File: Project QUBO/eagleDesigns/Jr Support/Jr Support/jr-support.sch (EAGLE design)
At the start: 173 parts, among them U1 PCA9685, U2 BME280

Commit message: 
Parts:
- added LED1, LED2, LED3, LED4, LED5, LED6, LED7: (no value), led:0805_LED
- added R20, R29, R32: 1.5k, resistor:R-US_R0805
- added R30, R31: 270, resistor:R-US_R0805
- added R33: 1.2k, resistor:R-US_R0805
- added R34: 68, resistor:R-US_R0805
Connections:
- new net N$68: LED1.A, R20.1
- new net N$69: LED2.A, R29.1
- new net N$70: LED3.A, R30.1
- new net N$71: LED4.A, R31.1
- new net N$72: LED5.A, R32.1
- new net N$73: LED6.A, R33.1
- new net N$74: LED7.A, R34.1
- net 12V: now also R33.2
- net GND: now also LED1.C, LED2.C, LED3.C, LED4.C, LED5.C, LED6.C, LED7.C
- net RELAY_OUT: now also R20.2
- net V_THRUST: now also R32.2
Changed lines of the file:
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@@
 <part name="R27" library="resistor" deviceset="R-US_" device="R0805" value="4.3k"/>
 <part name="R28" library="resistor" deviceset="R-US_" device="R0805" value="0"/>
+<part name="R20" library="resistor" deviceset="R-US_" device="R0805" value="1.5k"/>
+<part name="LED1" library="led" deviceset="0805_LED" device=""/>
+<part name="R29" library="resistor" deviceset="R-US_" device="R0805" value="1.5k"/>
+<part name="LED2" library="led" deviceset="0805_LED" device=""/>
+<part name="R30" library="resistor" deviceset="R-US_" device="R0805" value="270"/>
+<part name="LED3" library="led" deviceset="0805_LED" device=""/>
+<part name="R31" library="resistor" deviceset="R-US_" device="R0805" value="270"/>
+<part name="LED4" library="led" deviceset="0805_LED" device=""/>
+<part name="R32" library="resistor" deviceset="R-US_" device="R0805" value="1.5k"/>
+<part name="LED5" library="led" deviceset="0805_LED" device=""/>
+<part name="R33" library="resistor" deviceset="R-US_" device="R0805" value="1.2k"/>
+<part name="LED6" library="led" deviceset="0805_LED" device=""/>
+<part name="R34" library="resistor" deviceset="R-US_" device="R0805" value="68"/>
+<part name="LED7" library="led" deviceset="0805_LED" device=""/>
 </parts>
 <sheets>
@@
 <instance part="R27" gate="G$1" x="-375.92" y="35.56" rot="R270"/>
 <instance part="R28" gate="G$1" x="-342.9" y="17.78" rot="R90"/>
+<instance part="R20" gate="G$1" x="-213.36" y="68.58" rot="R90"/>
+<instance part="LED1" gate="G$1" x="-213.36" y="60.96"/>
+<instance part="R29" gate="G$1" x="-342.9" y="5.08" rot="R90"/>
+<instance part="LED2" gate="G$1" x="-342.9" y="-2.54"/>
+<instance part="R30" gate="G$1" x="-330.2" y="78.74" rot="R90"/>
+<instance part="LED3" gate="G$1" x="-330.2" y="71.12"/>
+<instance part="R31" gate="G$1" x="-45.72" y="-30.48" rot="R180"/>
+<instance part="LED4" gate="G$1" x="-38.1" y="-30.48" rot="R90"/>
+<instance part="R32" gate="G$1" x="-40.64" y="40.64" rot="R90"/>
+<instance part="LED5" gate="G$1" x="-40.64" y="33.02"/>
+<instance part="R33" gate="G$1" x="-40.64" y="111.76" rot="R90"/>
+<instance part="LED6" gate="G$1" x="-40.64" y="104.14"/>
+<instance part="R34" gate="G$1" x="241.3" y="81.28" rot="MR90"/>
+<instance part="LED7" gate="G$1" x="241.3" y="73.66" rot="MR0"/>
 </instances>
 <busses>
@@
 <wire x1="-228.6" y1="66.04" x2="-238.76" y2="66.04" width="0.1524" layer="91"/>
 <label x="-238.76" y="66.04" size="1.778" layer="95"/>
+<pinref part="LED1" gate="G$1" pin="C"/>
+<wire x1="-213.36" y1="55.88" x2="-228.6" y2="55.88" width="0.1524" layer="91"/>
+<wire x1="-228.6" y1="55.88" x2="-228.6" y2="66.04" width="0.1524" layer="91"/>
+<junction x="-228.6" y="66.04"/>
 </segment>
 <segment>
@@
 <label x="-360.68" y="10.16" size="1.778" layer="95"/>
 </segment>
+<segment>
+<pinref part="LED2" gate="G$1" pin="C"/>
+<wire x1="-342.9" y1="-7.62" x2="-358.14" y2="-7.62" width="0.1524" layer="91"/>
+<label x="-358.14" y="-7.62" size="1.778" layer="95"/>
+</segment>
+<segment>
+<pinref part="LED3" gate="G$1" pin="C"/>
+<wire x1="-330.2" y1="66.04" x2="-345.44" y2="66.04" width="0.1524" layer="91"/>
+<label x="-345.44" y="66.04" size="1.778" layer="95"/>
+</segment>
+<segment>
+<pinref part="LED4" gate="G$1" pin="C"/>
+<wire x1="-33.02" y1="-30.48" x2="-33.02" y2="-45.72" width="0.1524" layer="91"/>
+<label x="-33.02" y="-45.72" size="1.778" layer="95" rot="R90"/>
+</segment>
+<segment>
+<pinref part="LED5" gate="G$1" pin="C"/>
+<wire x1="-40.64" y1="27.94" x2="-55.88" y2="27.94" width="0.1524" layer="91"/>
+<label x="-55.88" y="27.94" size="1.778" layer="95"/>
+</segment>
+<segment>
+<pinref part="LED6" gate="G$1" pin="C"/>
+<wire x1="-40.64" y1="99.06" x2="-55.88" y2="99.06" width="0.1524" layer="91"/>
+<label x="-55.88" y="99.06" size="1.778" layer="95"/>
+</segment>
+<segment>
+<pinref part="LED7" gate="G$1" pin="C"/>
+<wire x1="241.3" y1="68.58" x2="256.54" y2="68.58" width="0.1524" layer="91"/>
+<label x="256.54" y="68.58" size="1.778" layer="95" rot="MR0"/>
+</segment>
 </net>
 <net name="5V-OUT" class="0">
@@
 <pinref part="C59" gate="G$1" pin="+"/>
 <wire x1="-251.46" y1="73.66" x2="-228.6" y2="73.66" width="0.1524" layer="91"/>
+<pinref part="R20" gate="G$1" pin="2"/>
+<wire x1="-228.6" y1="73.66" x2="-213.36" y2="73.66" width="0.1524" layer="91"/>
+<junction x="-228.6" y="73.66"/>
 </segment>
 <segment>
@@
 <segment>
 <pinref part="U$36" gate="G$1" pin="P$2"/>
-<wire x1="-58.42" y1="116.84" x2="-53.34" y2="116.84" width="0.1524" layer="91"/>
 <label x="-55.88" y="116.84" size="1.778" layer="95"/>
 <pinref part="U$49" gate="G$1" pin="C"/>
 <wire x1="-58.42" y1="106.68" x2="-58.42" y2="116.84" width="0.1524" layer="91"/>
 <junction x="-58.42" y="116.84"/>
+<pinref part="R33" gate="G$1" pin="2"/>
+<wire x1="-58.42" y1="116.84" x2="-40.64" y2="116.84" width="0.1524" layer="91"/>
 </segment>
 <segment>
@@
 <segment>
 <pinref part="U$5" gate="G$1" pin="P$2"/>
-<wire x1="-60.96" y1="45.72" x2="-53.34" y2="45.72" width="0.1524" layer="91"/>
 <label x="-58.42" y="45.72" size="1.778" layer="95"/>
 <pinref part="U$38" gate="G$1" pin="C"/>
 <wire x1="-60.96" y1="35.56" x2="-60.96" y2="45.72" width="0.1524" layer="91"/>
 <junction x="-60.96" y="45.72"/>
+<pinref part="R32" gate="G$1" pin="2"/>
+<wire x1="-60.96" y1="45.72" x2="-40.64" y2="45.72" width="0.1524" layer="91"/>
 </segment>
 <segment>
@@
 </segment>
 </net>
+<net name="N$68" class="0">
+<segment>
+<pinref part="R20" gate="G$1" pin="1"/>
+<pinref part="LED1" gate="G$1" pin="A"/>
+</segment>
+</net>
+<net name="N$69" class="0">
+<segment>
+<pinref part="R29" gate="G$1" pin="1"/>
+<pinref part="LED2" gate="G$1" pin="A"/>
+</segment>
+</net>
+<net name="N$70" class="0">
+<segment>
+<pinref part="R30" gate="G$1" pin="1"/>
+<pinref part="LED3" gate="G$1" pin="A"/>
+</segment>
+</net>
+<net name="N$71" class="0">
+<segment>
+<pinref part="R31" gate="G$1" pin="1"/>
+<pinref part="LED4" gate="G$1" pin="A"/>
+</segment>
+</net>
+<net name="N$72" class="0">
+<segment>
+<pinref part="R32" gate="G$1" pin="1"/>
+<pinref part="LED5" gate="G$1" pin="A"/>
+</segment>
+</net>
+<net name="N$73" class="0">
+<segment>
+<pinref part="R33" gate="G$1" pin="1"/>
+<pinref part="LED6" gate="G$1" pin="A"/>
+</segment>
+</net>
+<net name="N$74" class="0">
+<segment>
+<pinref part="R34" gate="G$1" pin="1"/>
+<pinref part="LED7" gate="G$1" pin="A"/>
+</segment>
+</net>

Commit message: 
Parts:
- removed 2PIN_5: (no value), molex:KK254_VERT_2PIN22-29-2021
- removed 5V_REG: 21k, resistor:R-US_R0805
- removed LED3: (no value), led:0805_LED
- removed R25: 100, resistor:R-US_R0805
- removed R30: 270, resistor:R-US_R0805
- removed U$55, U$57: NCP1117, ONSemi:NCP1117
- removed U$56: 74LVC1G14, NXP:74LVC1G14
- removed U$58: VTVS, diode:VTVS
- added C28: 15p, resistor:C-USC0805
- added C35: 22u, resistor:C-USC0805
- added C65: 0.1u, resistor:C-USC0805
- added L2: 2.2u, resistor:L-USL0740
- C27: value 100u -> 10u; device resistor:CPOL-USE3.5-8 -> resistor:C-USC0805
- C34, C38, C39, C63: value 10u -> 1u
- C36: value 0.1u -> 220u; device resistor:C-USC0805 -> resistor:CPOL-USC-F80
- C4: value 100u -> 1u; device resistor:CPOL-USF -> resistor:C-USC0805
- C40: value 2.2u -> 10u
- C41: value 2.2u -> 0.1u
- C42: value 1u -> 15p
- C61: value 10u -> 22u
- C62: value 10u -> 220u; device resistor:C-USC0805 -> resistor:CPOL-USC-F80
- L1: value 3.3u -> 2.2u; device resistor:L-USHCMA0703 -> resistor:L-USL0740
- R14: value 1.5k -> 41.2k
- R15: value 1k -> 1M
- R16: value 7.15k -> 88.7k
- R17: value 8m -> 41.2k
- R23: value 510 -> 1M
- R24: value 6.8k -> 243k
- U$1: value PTN78060W -> LT8640; device texas:PTN78060W -> linear:LT8640
- U$24: value LTM4605 -> LT8640; device linear:LTM4605 -> linear:LT8640
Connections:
- removed net 5V-OUT: U$1.VO
- removed net N$49: C60.1, R23.2, U$56.IN
- removed net N$50: 2PIN_5.P$1, R23.1, R24.1, U$58.C
- removed net N$58: C27.+, U$24.VOUT, U$35.IP+
- removed net N$62: C63.1, R25.1, U$55.VOUT
- removed net N$63: R25.2, U$1.!INHIBIT!
- removed net N$70: LED3.A, R30.1
- removed net RELAY_CTRL: U$56.OUT
- removed net V_BATT1: C61.1, U$57.VIN
- net CPU_ON: now also U$1.EN/UV; no longer U$24.RUN
- net GND: now also C27.2, C35.2, C36.-, C4.2, C60.2, C62.-, R14.1, R24.1, U$1.GND, U$1.GND-1, U$1.GND-2, U$24.GND, U$24.GND-1, U$24.GND-2; no longer 5V_REG.2, C27.-, C36.2, C4.-, C41.2, C42.2, C62.2, LED3.C, R15.1, U$1.GND1, U$1.GND2, U$24.FCB, U$24.PGND, U$24.SENSE-, U$24.SGND, U$55.GND, U$57.GND
- net N$1: now also R14.2, U$1.RT; no longer 5V_REG.1, U$1.VOADJUST
- net N$32: now also C41.2, L2.1, U$1.SW; no longer L1.1, U$24.SW1
- net N$40: now also C65.2, L1.1, U$24.SW; no longer R14.2, U$24.INTV_CC
- net N$42: now also C42.2, R23.1, R24.2, U$24.FB; no longer R14.1, R15.2, U$24.PLLFLTR
- net N$43: now also C65.1, U$24.BST; no longer R16.2, U$24.V_FB
- net N$44: now also C28.2, R15.1, R16.2, U$1.FB; no longer R17.2, U$24.R_SENSE, U$24.SENSE+
- net N$45: now also C41.1, U$1.BST; no longer C36.1, U$24.SS
- net N$46: now also C42.1, C61.1, C62.+, R23.2, U$2.IP+, U$24.BIAS; no longer U$24.SW2
- net N$48: now also C63.1, U$24.INTV-CC; no longer 2PIN_5.P$2, C60.2, U$56.GND, U$58.A
- net N$54: now also C39.1, U$1.INTV-CC; no longer C62.1, R24.2, U$56.VDD, U$57.VOUT
- net N$7: now also C28.1, C35.1, C36.+, L2.2, R15.2, U$1.BIAS, U$35.IP+; no longer U$1.VOSENSE
- net N$8: now also R17.2, U$24.RT; no longer C4.+, C40.1, U$2.IP+
- net RELAY_OUT: now also C27.1, C4.1, C40.1, C60.1, U$1.VIN-1, U$1.VIN-2, U$24.EN/UV, U$24.VIN-1, U$24.VIN-2; no longer C39.1, C41.1, C42.1, U$1.VI, U$24.VIN, U$55.VIN
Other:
- note added: "PG is an open-drain fault pin."
- note removed: "RUN is an enable-high pin (max 6V) to turn on the regulator."
- moved on the sheet: 2PIN_3, C32, C34, C38, C39, C40, C41, C42, C60, C61, C63, L1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

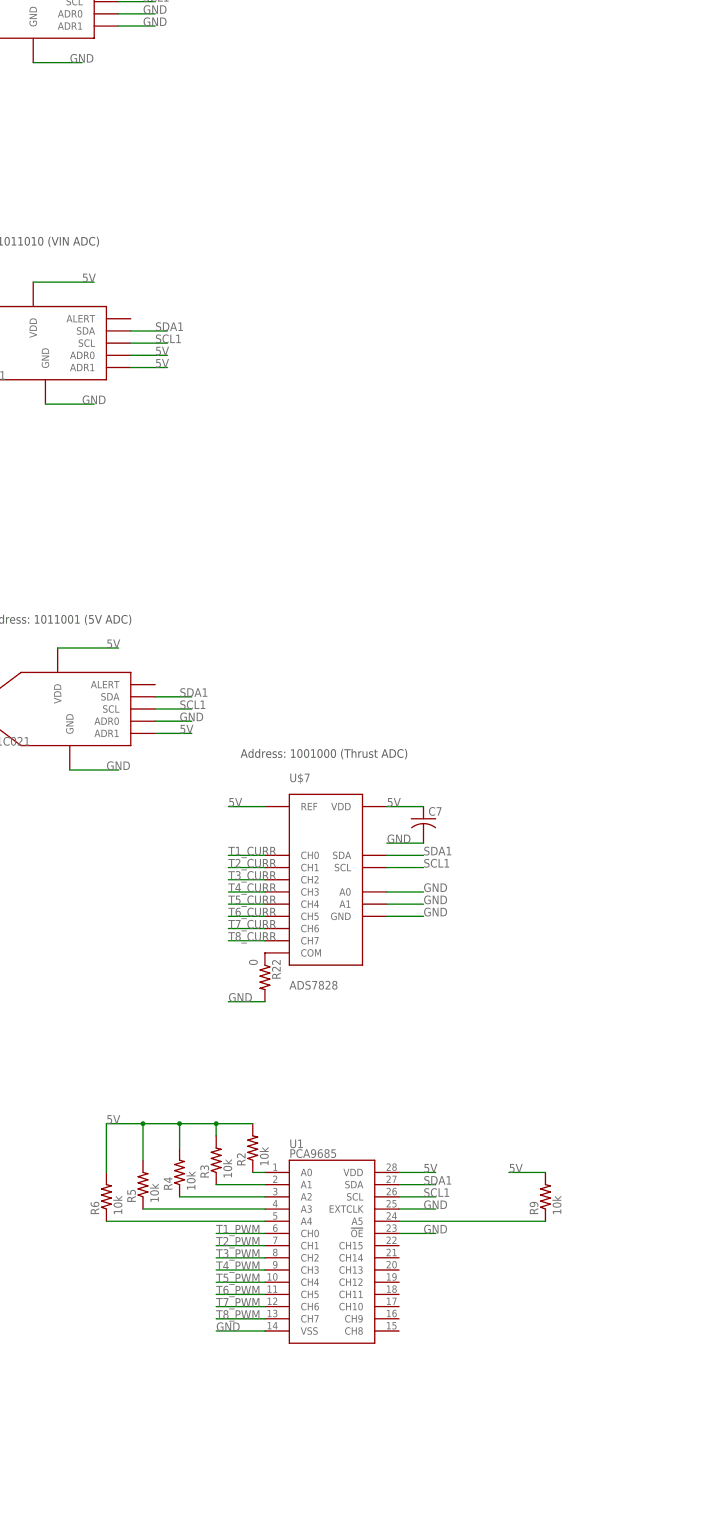
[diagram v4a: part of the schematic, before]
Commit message: Added INA219 voltage sensors.
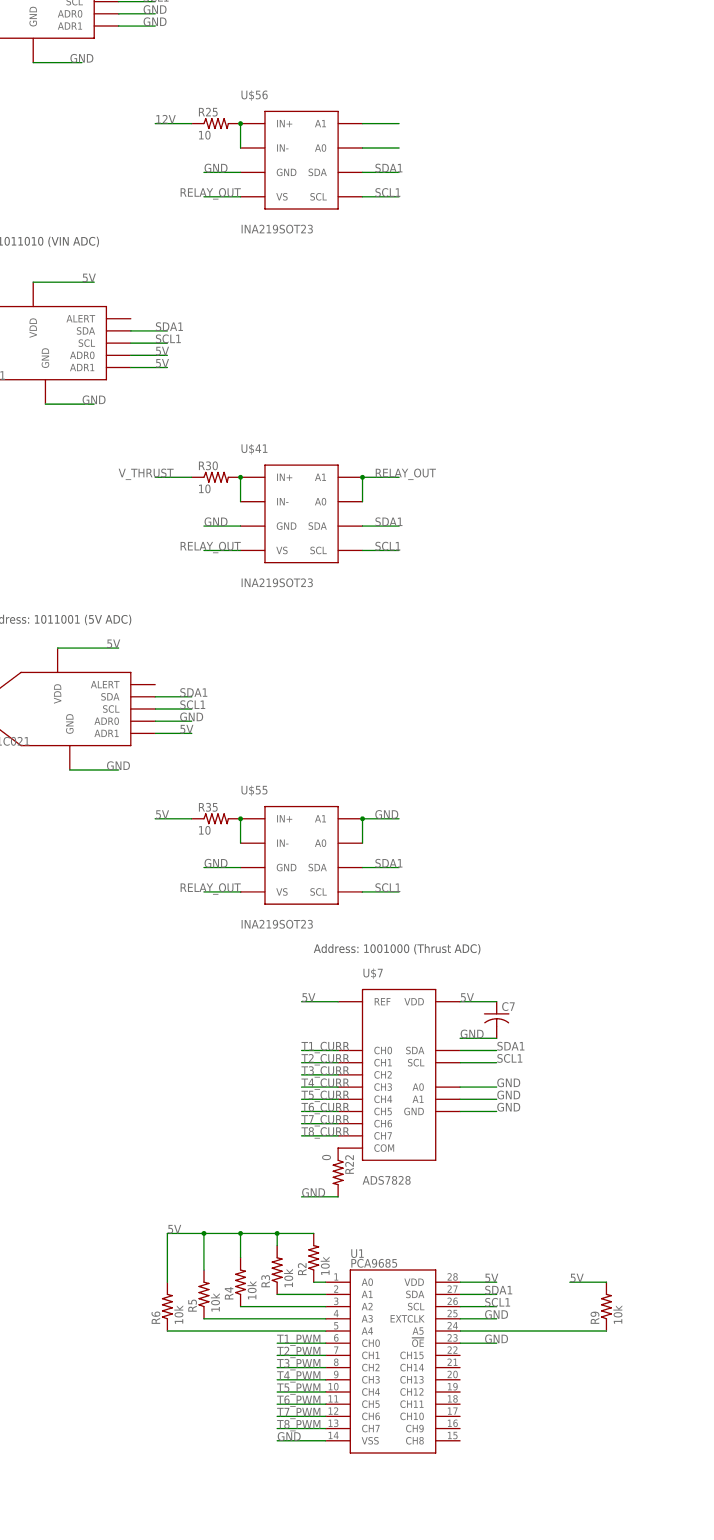
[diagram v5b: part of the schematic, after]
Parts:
- added R25, R30, R35: 10, resistor:R-US_R0805
- added U$41, U$55, U$56: INA219SOT23, texas:INA219SOT23
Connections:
- new net N$49: R25.2, U$56.IN+, U$56.IN-
- new net N$58: R30.2, U$41.IN+, U$41.IN-
- new net N$77: R35.2, U$55.IN+, U$55.IN-
- net 12V: now also R25.1
- net 5V: now also R35.1
- net GND: now also U$41.GND, U$55.A0, U$55.A1, U$55.GND, U$56.A0, U$56.GND
- net RELAY_OUT: now also U$41.A0, U$41.A1, U$41.VS, U$55.VS, U$56.A1, U$56.VS
- net SCL1: now also U$41.SCL, U$55.SCL, U$56.SCL
- net SDA1: now also U$41.SDA, U$55.SDA, U$56.SDA
- net V_THRUST: now also R30.1
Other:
- moved on the sheet: C7, R2, R22, R3, R4, R5, R6, R9, U$7, U1

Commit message: 
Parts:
- removed 2PIN_3: (no value), molex:KK254_VERT_2PIN22-29-2021
- removed LED4, LED5, LED6, LED7: (no value), led:0805_LED
- added 12V_LED, 3V3_LED, 5V_LED, BATTERY_LED, RELAY-OUT_LED, SHORE_LED, V-THRUST_LED: (no value), led:0805_LED
- added C66: 2.2u, resistor:C-USC0805
- added C67, C68: (no value), resistor:C-USC0805
- added CPU_ON, FAN1: KK254_VERT_2PIN22-29-2021, molex:KK254_VERT_2PIN22-29-2021
- added FAN2: Ethernet switch pwr, molex:KK254_VERT_2PIN22-29-2021
- added R36: 43k, resistor:R-US_R0805
- added R37: 4.3k, resistor:R-US_R0805
- added R38: 1.2k, resistor:R-US_R0805
- added R39: 1.5k, resistor:R-US_R0805
- added R40: 50k, resistor:R-US_R0805
- added SHORE-FET: IPD50P04P4-13, transistor-power:IPD50P04P4-13
- added SHORE_IN: 2_SUPERSABRE, molex:2_SUPERSABRE
- added U$57: VTVS, diode:VTVS
- added U$58, U$66: DMP32D5SFB, transistor-fet:DMP32D5SFB
- added U$63: GPTS203212B, switches:GPTS203212B
- added U$64, U$65: DESD, diode:DESD
- CAMERA1: value Camera1 pwr -> KK254_VERT_2PIN22-29-2021
- CAMERA2: value Camera2\ pwr -> KK254_VERT_2PIN22-29-2021
- ETHERNET: value Ethernet switch pwr -> KK254_VERT_2PIN22-29-2021
- LED1, LED2: value (none) -> FASTCHG; device led:0805_LED -> led:LEDCHIP-LED0805
- R13: value 0 -> 1.2k
- R28: value 0 -> 50k
- THRUST1, THRUST2, THRUST3, THRUST4, THRUST5, THRUST6, THRUST7, THRUST8: value (none) -> KK254_VERT_4PIN22-29-2041
- renumbered 2PIN_1 to CAMERA1, 2PIN_10 to CAMERA2, 2PIN_4 to ETHERNET, 2PIN_7 to V-THRUST_OUT, 2PIN_8 to 12V_OUT, 2PIN_9 to 5V_OUT, 4PIN_1 to THRUST1, 4PIN_10 to THRUST8, 4PIN_2 to THRUST2, 4PIN_3 to THRUST3, 4PIN_4 to THRUST4, 4PIN_5 to THRUST5, 4PIN_6 to THRUST6, 4PIN_7 to THRUST7, 4PIN_8 to DEPTH_SENS, 4PIN_9 to CPU_PWR, U$1 to 12V_REG, U$21 to I2C_SHIFT, U$24 to 5V_REG, U$41 to V-THRUST_VOLAGE, U$42 to 5V_CURR_ADC, U$43 to V-THRUST_CURR_ADC, U$44 to 12V_CURR_ADC, U$55 to 5V_VOLTAGE, U$56 to 12V_VOLTAGE, U$7 to THRUSTER_CURR_ADC, U2 to BME280, VIN to BATTERY_IN
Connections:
- removed net N$46: 5V_REG.BIAS, C42.1, C61.1, C62.+, L1.2, R23.2, U$2.IP+
- new net N$50: R37.1, SHORE-FET.D, SHORE_IN.P$1, U$57.C
- new net N$62: C66.1, R36.1, SHORE-FET.G
- new net N$63: R36.2, R37.2, U$63.P$2
- new net N$70: R13.2, U$58.D
- new net N$75: R39.1, SHORE_LED.A
- new net N$76: 5V_REG.PG, R28.1, U$58.G
- new net N$78: LED2.A, R38.1
- new net N$79: R38.2, U$66.D
- new net N$80: 12V_REG.PG, R40.1, U$66.G
- new net SW-5V: 5V_REG.BIAS, C2.1, C42.1, C61.1, C62.+, L1.2, R23.2, U$2.IP+, U$2.VCC
- net 3V3: now also R34.2
- net 5V: now also C67.1, C68.1, FAN1.P$1, FAN2.P$1, R31.2, U$64.C, U$65.C; no longer C2.1, U$2.VCC
- net GND: now also 12V_LED.C, 3V3_LED.C, 5V_LED.C, BATTERY_LED.C, C66.2, C67.2, C68.2, FAN1.P$2, FAN2.P$2, RELAY-OUT_LED.C, SHORE_IN.P$2, SHORE_LED.C, U$57.A, U$63.P$1, U$64.A, U$65.A, V-THRUST_LED.C; no longer LED4.C, LED5.C, LED6.C, LED7.C, R13.1
- net N$26: now also U$22.C
- net N$51: now also CPU_ON.P$2; no longer 2PIN_3.P$2
- net N$53: now also U$19.VIOUT
- net N$60: now also U$35.VIOUT
- net N$61: now also CPU_ON.P$1; no longer 2PIN_3.P$1
- net N$67: now also LED1.A, R13.1; no longer R28.2, U$61.S
- net N$68: now also RELAY-OUT_LED.A; no longer LED1.A
- net N$69: now also BATTERY_LED.A; no longer LED2.A
- net N$71: now also 5V_LED.A; no longer LED4.A
- net N$72: now also V-THRUST_LED.A; no longer LED5.A
- net N$73: now also 12V_LED.A; no longer LED6.A
- net N$74: now also 3V3_LED.A; no longer LED7.A
- net RELAY-BATT: now also R29.2, U$61.S; no longer R28.1
- net RELAY-SHORE: now also R39.2, SHORE-FET.S; no longer R13.2
- net RELAY_OUT: now also R28.2, R40.2, U$58.S, U$66.S
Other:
- note added: "Should these be 5V powered?"
- moved on the sheet: C32, LED1, LED2, R13, R18, R21, R28, U$45, U$59

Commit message: Main switch added to Jr Support.
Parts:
- added C69, C71, C73, C75: 100nF, resistor:C-USC0805
- added C70, C74: 10nF, resistor:C-USC0805
- added C72, C76: T491D475K050AT, resistor:CPOL-USCT7343
- added D1: MMSD4148, diode:DIODE-SOD123
- added IC1, IC3: 74LVC1G08DBV, 74xx-little-us:74LVC1G08DBV
- added IC2: TLC2272D, texas:TLC2272D
- added LED3: Green, led:LEDCHIP-LED0805
- added N1: 2N7002, transistor-fet:2N7002
- added OFF, ON: DTS-6, switch-tact:DTS-6
- added OFF_SW, ON_SW, T_FUSE, WATER: (no value), pinhead:PINHD-1X2
- added Q1: FDN5618P, transistor-fet:FDN5618P
- added R41, R42, R45, R53, R54: 10k, resistor:R-US_R0805
- added R43: 845k, resistor:R-US_R0805
- added R44, R50: 115k, resistor:R-US_R0805
- added R46, R49, R51: 1M, resistor:R-US_R0805
- added R47, R48: 3.3k, resistor:R-US_R0805
- added R52, R55, R57, R58: 100k, resistor:R-US_R0805
- added R56: 470, resistor:R-US_R0805
- added R59: (no value), resistor:R-TRIMM3314J
- added SK_DISABLE, SK_DISABLE1, TH_DISABLE: (no value), jumper:JP1E
- added U2, U3: LT3063, linear:LT3063
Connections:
- new net +5V: C69.1, C71.1, IC2P.VCC, IC3P.VCC, R43.2, R55.1, R57.2, R59.A, SK_DISABLE.2, TH_DISABLE.2, T_FUSE.1, U2.OUT
- new net FAULT: IC1A.O, IC3A.I1, OFF.3, OFF.4, OFF_SW.1
- new net FET: IC3A.O, N1.G, R53.2
- new net N$46: Q1.G, R41.1, R42.1
- new net N$81: D1.A, N1.D, R42.2
- new net N$82: R43.1, R44.2, U2.ADJ
- new net N$83: C70.1, U2.REF/BYP
- new net N$84: LED3.A, R47.1, R48.1
- new net N$85: R49.1, R50.2, U3.ADJ
- new net N$86: C74.1, U3.REF/BYP
- new net N$87: IC1A.I1, R51.2, TH_DISABLE.1, T_FUSE.2
- new net N$88: IC2A.-IN, IC2B.OUT, R52.1
- new net N$89: IC2B.-IN, R52.2, R54.1
- new net N$90: IC2B.+IN, R57.1, R58.2
- new net N$91: R54.2, R55.2, R56.1
- new net N$92: R56.2, WATER.1
- new net N$93: IC2A.+IN, R59.S
- new net N$94: IC2A.OUT, SK_DISABLE1.1
- new net ON_SW: D1.C, ON.3, ON.4, ON_SW.1
- new net SK: C73.1, IC3A.I0, R45.1, R46.2, SK_DISABLE.1
- new net SOFT_KILL: R45.2
- new net VDD: C72.+, C76.+, Q1.D, R47.2, R48.2, U2.IN, U2.SHDN, U3.IN, U3.SHDN
- new net WATER: IC1A.I0, SK_DISABLE1.2
- net GND: now also C69.2, C70.2, C71.2, C72.-, C73.2, C74.2, C75.2, C76.-, IC2P.GND, IC3P.GND, LED3.C, N1.S, OFF.1, OFF.2, OFF_SW.2, ON.1, ON.2, ON_SW.2, R44.1, R46.1, R50.1, R51.1, R53.1, R58.1, R59.E, U2.GND, U3.GND, WATER.2
- net RELAY-BATT: now also Q1.S, R41.2
- net RELAY-CTRL: now also C75.1, R49.2, U3.OUT
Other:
- note added: "10V LDO"
- note added: "5V LDO"
- note added: "Main Gate Control"
- note added: "Off Switch"
- note added: "On Indicator"
- note added: "On Switch"
- note added: "Power Switching"
- note added: "Secondary AND Gate"
- note added: "Water Sensor Amplifier"

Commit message: 
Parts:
- R10, R11: value 10k -> 4.2k
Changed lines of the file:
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@@
 <part name="CAMERA1" library="molex" deviceset="KK254_VERT_2PIN" device="22-29-2021"/>
 <part name="I2C_SHIFT" library="texas" deviceset="PCA9306" device="DCT"/>
-<part name="R10" library="resistor" deviceset="R-US_" device="R0805" value="10k"/>
-<part name="R11" library="resistor" deviceset="R-US_" device="R0805" value="10k"/>
+<part name="R10" library="resistor" deviceset="R-US_" device="R0805" value="4.2k"/>
+<part name="R11" library="resistor" deviceset="R-US_" device="R0805" value="4.2k"/>
 <part name="R12" library="resistor" deviceset="R-US_" device="R0805" value="200k"/>
 <part name="ETHERNET" library="molex" deviceset="KK254_VERT_2PIN" device="22-29-2021"/>
